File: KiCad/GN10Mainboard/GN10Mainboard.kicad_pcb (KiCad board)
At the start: 4 copper layers, 70 x 50 mm, 106 parts, among them J1 XT30PW-M, J10 Conn_01x05_Socket, J2 Conn_01x02_Pin, J3 USB_C_Receptacle_USB2.0_16P, J4 Conn_01x04, J5 Conn_01x04, J6 Conn_01x04, J7 Conn_01x04, J8 Conn_01x04, J9 Conn_01x06, SW1 SW_Push, SW2 SW_DIP_x04, SW3 SW_Push, U1 OKL-T/x-W5N-C, U2 3.3V, U3 STM32G474RCTx, U4 TBD62083AFNG, U5 7segmentLED, U6 RNBD451, U7 FT231XS, U8 MCP2562-E-SN, U9 MCP2562-E-SN, Y1 24MHz, Y2 32.768kHz

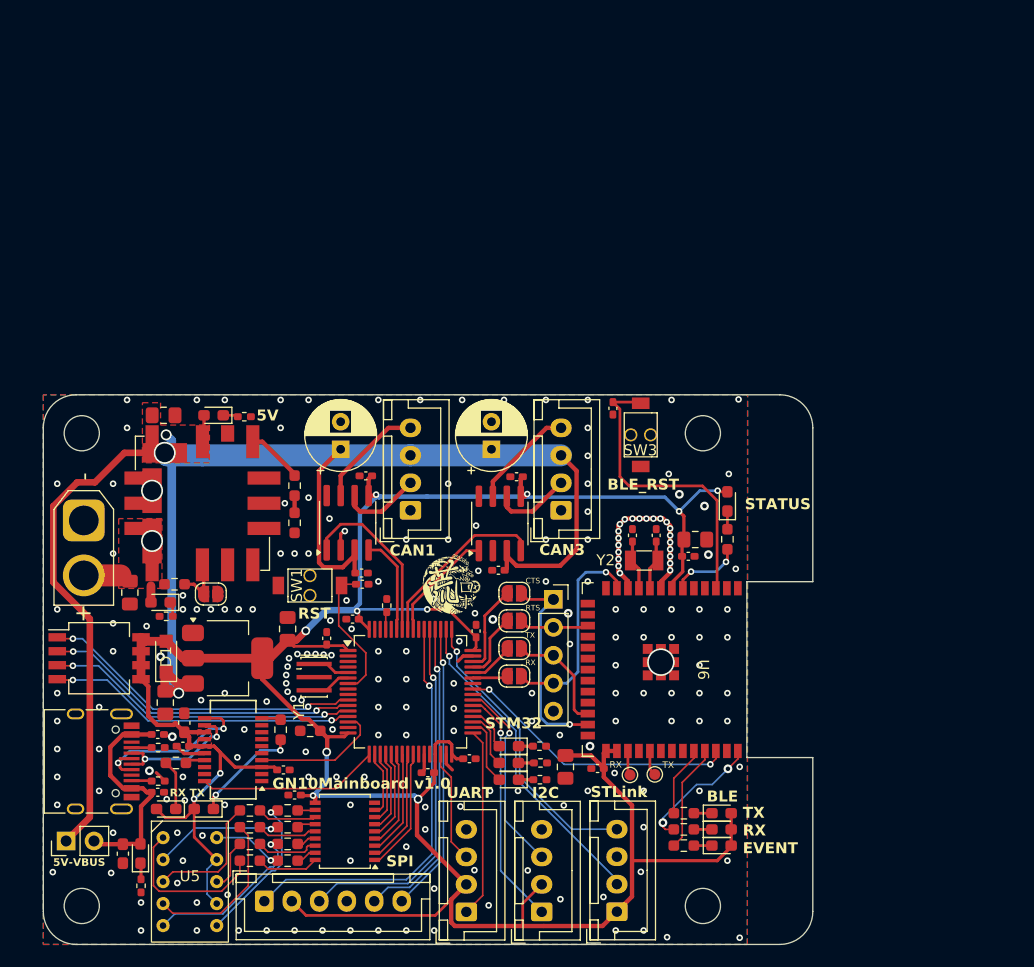
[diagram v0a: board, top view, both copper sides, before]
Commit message: Optimized PCB layout for better noise suppression
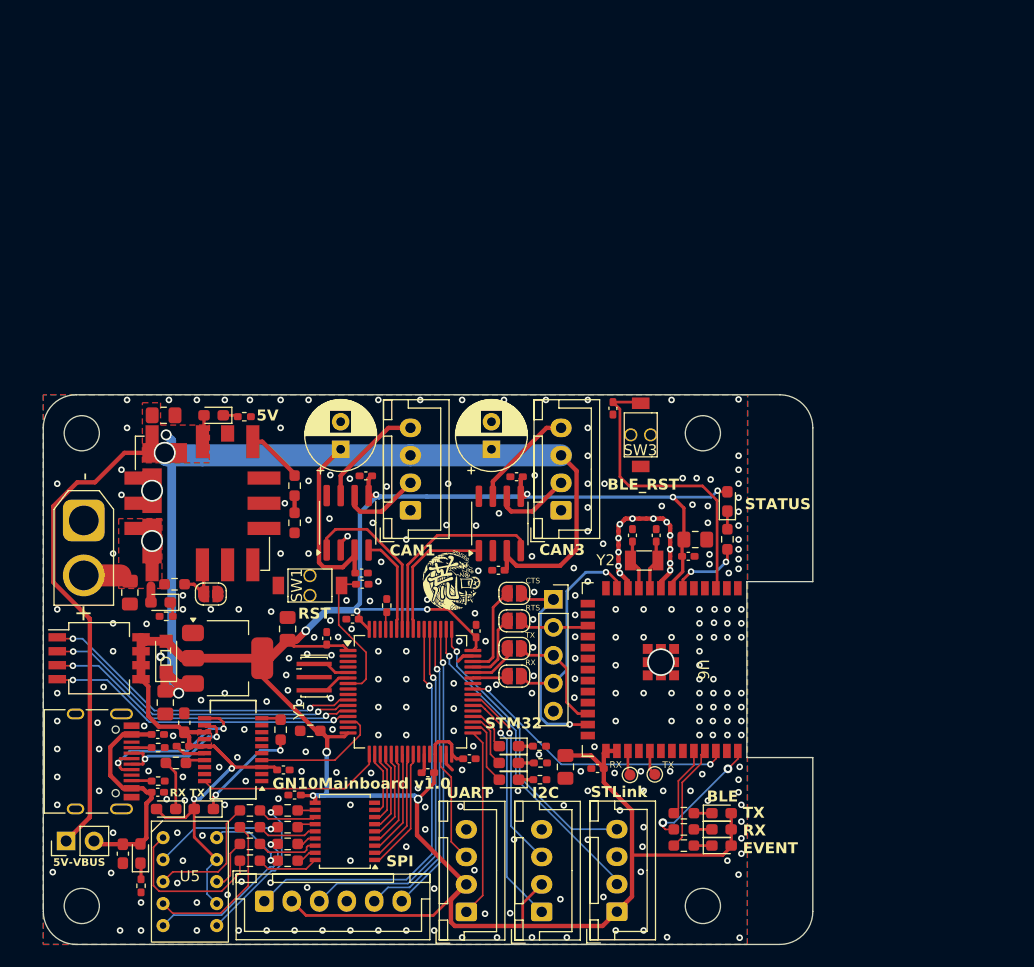
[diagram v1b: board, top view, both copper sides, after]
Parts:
- moved G*** 0.36 mm to (167.0, 117.1)
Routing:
- net +3.3V: track 284.1 -> 286.5 mm
- net CAN3_RX: track 10.3 -> 12.3 mm
- net CAN3_TX: track 16.4 -> 18.4 mm
- net GND: track 28.5 -> 26.8 mm, vias 211 -> 287
- net LED_B_DRV: track 6.41 -> 7.20 mm
- net BLE_UART_RX: track 19.0 -> 18.3 mm

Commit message: 2layer PCB version
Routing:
- removed copper zone on In1.Cu, net GND
- removed copper zone on In2.Cu, net GND
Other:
- copper layers 4 -> 2
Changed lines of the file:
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@@
 	(layers
 		(0 "F.Cu" signal)
-		(1 "In1.Cu" signal)
-		(2 "In2.Cu" signal)
 		(31 "B.Cu" signal)
 		(32 "B.Adhes" user "B.Adhesive")
@@
 			)
 			(layer "dielectric 1"
-				(type "prepreg")
-				(thickness 0.1)
-				(material "FR4")
-				(epsilon_r 4.5)
-				(loss_tangent 0.02)
-			)
-			(layer "In1.Cu"
-				(type "copper")
-				(thickness 0.035)
-			)
-			(layer "dielectric 2"
 				(type "core")
-				(thickness 1.24)
-				(material "FR4")
-				(epsilon_r 4.5)
-				(loss_tangent 0.02)
-			)
-			(layer "In2.Cu"
-				(type "copper")
-				(thickness 0.035)
-			)
-			(layer "dielectric 3"
-				(type "prepreg")
-				(thickness 0.1)
+				(thickness 1.51)
 				(material "FR4")
 				(epsilon_r 4.5)
@@
 			(drillshape 0)
 			(scaleselection 1)
-			(outputdirectory "GN10Mainboard_4layer_v1.0")
+			(outputdirectory "GN10Mainboard_2layer_v1.0")
 		)
 	)
@@
 		(net 1)
 		(net_name "GND")
-		(layers "F.Cu" "In1.Cu" "In2.Cu" "B.Cu")
+		(layers "F&B.Cu")
 		(hatch edge 0.5)
 		(connect_pads thru_hole_only
@@
 		(net 0)
 		(net_name "")
-		(layers "F.Cu" "In1.Cu" "In2.Cu" "B.Cu" "Cmts.User")
+		(layers "F&B.Cu" "Cmts.User")
 		(hatch edge 0.5)
 		(connect_pads

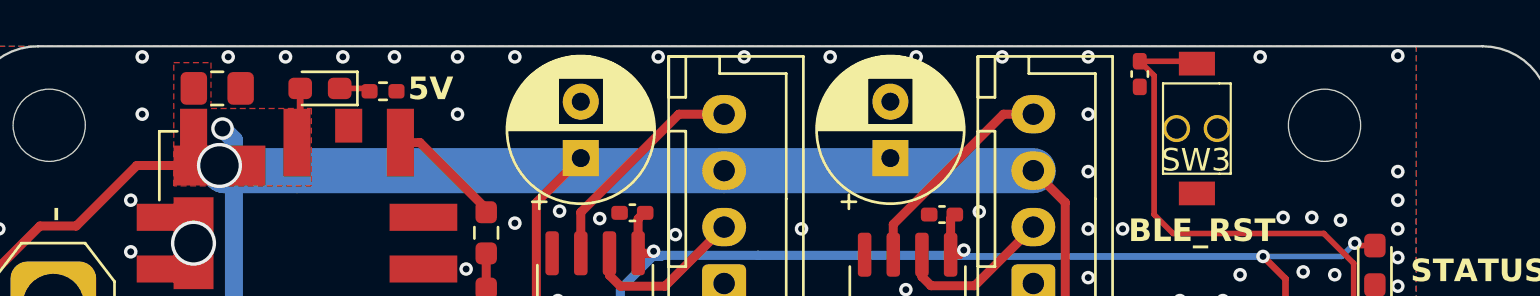
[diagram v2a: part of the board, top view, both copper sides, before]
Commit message: fix: PCB design rules.
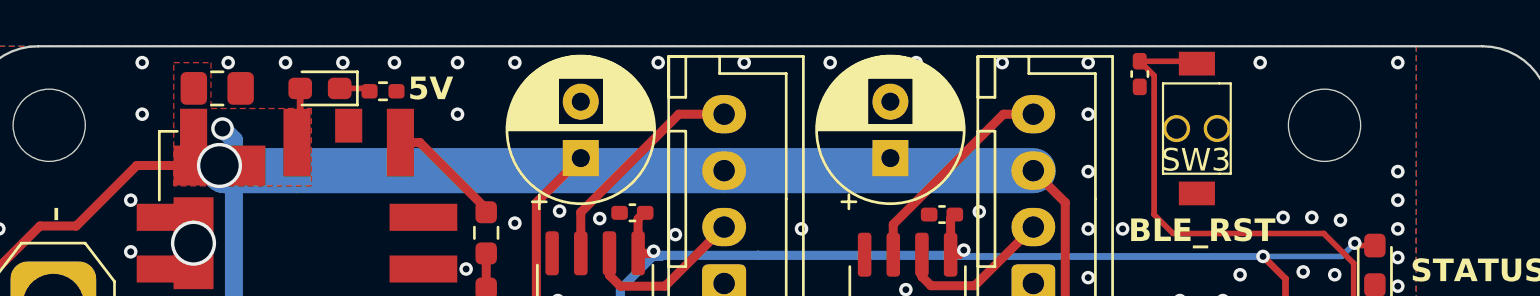
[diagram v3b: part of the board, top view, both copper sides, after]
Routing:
- added copper zone on In1.Cu, net GND
- added copper zone on In2.Cu, net GND
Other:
- copper layers 2 -> 4
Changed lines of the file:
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@@
 	(layers
 		(0 "F.Cu" signal)
+		(1 "In1.Cu" signal)
+		(2 "In2.Cu" signal)
 		(31 "B.Cu" signal)
 		(32 "B.Adhes" user "B.Adhesive")
@@
 			)
 			(layer "dielectric 1"
+				(type "prepreg")
+				(thickness 0.1)
+				(material "FR4")
+				(epsilon_r 4.5)
+				(loss_tangent 0.02)
+			)
+			(layer "In1.Cu"
+				(type "copper")
+				(thickness 0.035)
+			)
+			(layer "dielectric 2"
 				(type "core")
-				(thickness 1.51)
+				(thickness 1.24)
+				(material "FR4")
+				(epsilon_r 4.5)
+				(loss_tangent 0.02)
+			)
+			(layer "In2.Cu"
+				(type "copper")
+				(thickness 0.035)
+			)
+			(layer "dielectric 3"
+				(type "prepreg")
+				(thickness 0.1)
 				(material "FR4")
 				(epsilon_r 4.5)
@@
 			(drillshape 0)
 			(scaleselection 1)
-			(outputdirectory "GN10Mainboard_2layer_v1.0")
+			(outputdirectory "GN10Mainboard_4layer_v1.0")
 		)
 	)
@@
 	)
 	(via
-		(at 137.62 100.47)
+		(at 137.62 100.724)
 		(size 0.6)
 		(drill 0.3)
@@
 	)
 	(via
-		(at 171.91 100.47)
+		(at 171.91 100.724)
 		(size 0.6)
 		(drill 0.3)
@@
 	)
 	(via
-		(at 193.246 100.4192)
+		(at 193.246 100.724)
 		(size 0.6)
 		(drill 0.3)
@@
 	)
 	(via
-		(at 148.796 100.47)
+		(at 148.796 100.724)
 		(size 0.6)
 		(drill 0.3)
@@
 	)
 	(via
-		(at 168.1 100.47)
+		(at 168.1 100.724)
 		(size 0.6)
 		(drill 0.3)
@@
 	)
 	(via
-		(at 179.53 100.47)
+		(at 179.53 100.724)
 		(size 0.6)
 		(drill 0.3)
@@
 	)
 	(via
-		(at 141.43 100.47)
+		(at 141.43 100.724)
 		(size 0.6)
 		(drill 0.3)
@@
 	)
 	(via
-		(at 164.29 100.47)
+		(at 164.29 100.724)
 		(size 0.6)
 		(drill 0.3)
@@
 	)
 	(via
-		(at 160.48 100.47)
+		(at 160.48 100.724)
 		(size 0.6)
 		(drill 0.3)
@@
 	)
 	(via
-		(at 143.97 100.47)
+		(at 143.97 100.724)
 		(size 0.6)
 		(drill 0.3)
@@
 	)
 	(via
-		(at 187.15 100.47)
+		(at 187.15 100.724)
 		(size 0.6)
 		(drill 0.3)
@@
 	)
 	(via
-		(at 154.13 100.47)
+		(at 154.13 100.724)
 		(size 0.6)
 		(drill 0.3)
@@
 	)
 	(via
-		(at 146.51 100.47)
+		(at 146.51 100.724)
 		(size 0.6)
 		(drill 0.3)
@@
 	)
 	(via
-		(at 175.72 100.47)
+		(at 175.72 100.724)
 		(size 0.6)
 		(drill 0.3)
@@
 	)
 	(via
-		(at 151.59 100.47)
+		(at 151.59 100.724)
 		(size 0.6)
 		(drill 0.3)
@@
 		(net 1)
 		(net_name "GND")
-		(layers "F&B.Cu")
+		(layers "F.Cu" "In1.Cu" "In2.Cu" "B.Cu")
 		(hatch edge 0.5)
 		(connect_pads thru_hole_only

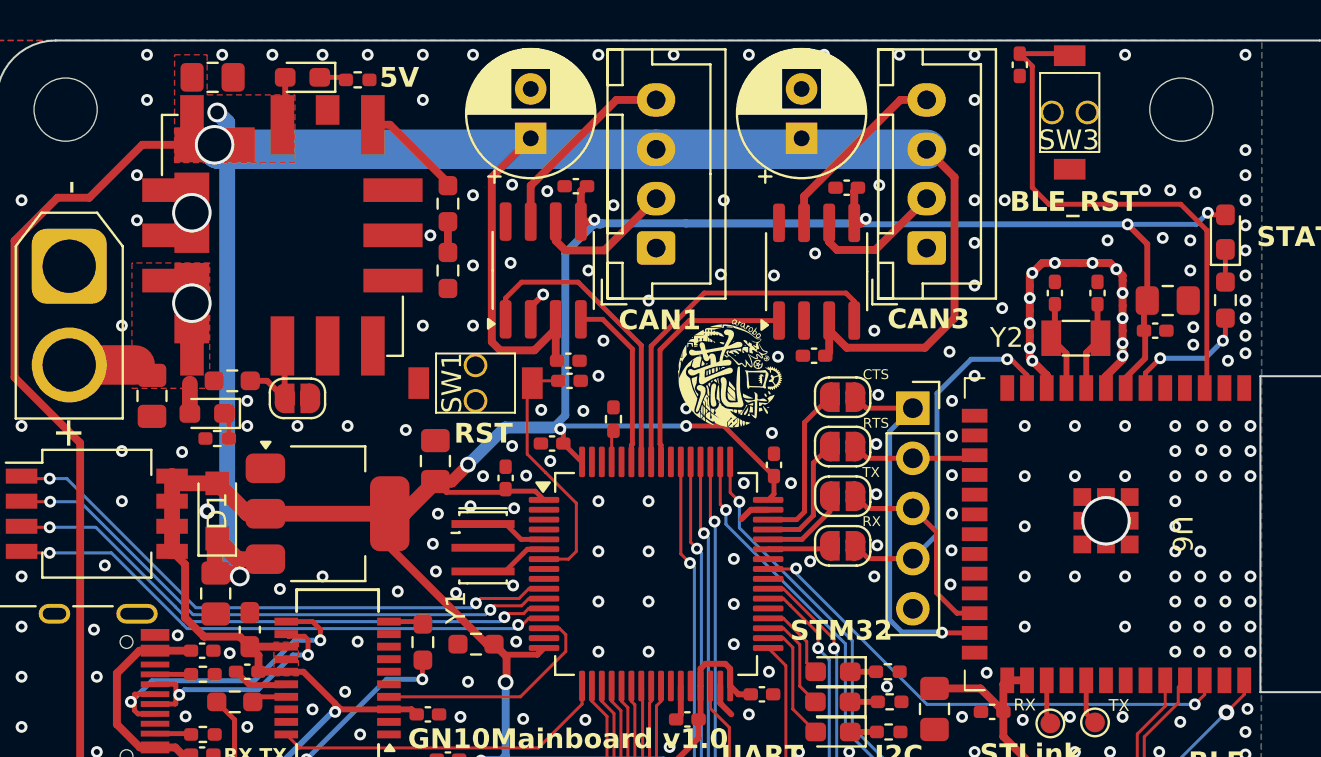
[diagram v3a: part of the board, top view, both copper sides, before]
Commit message: fix:CAN tx/rx pin & silkscreen
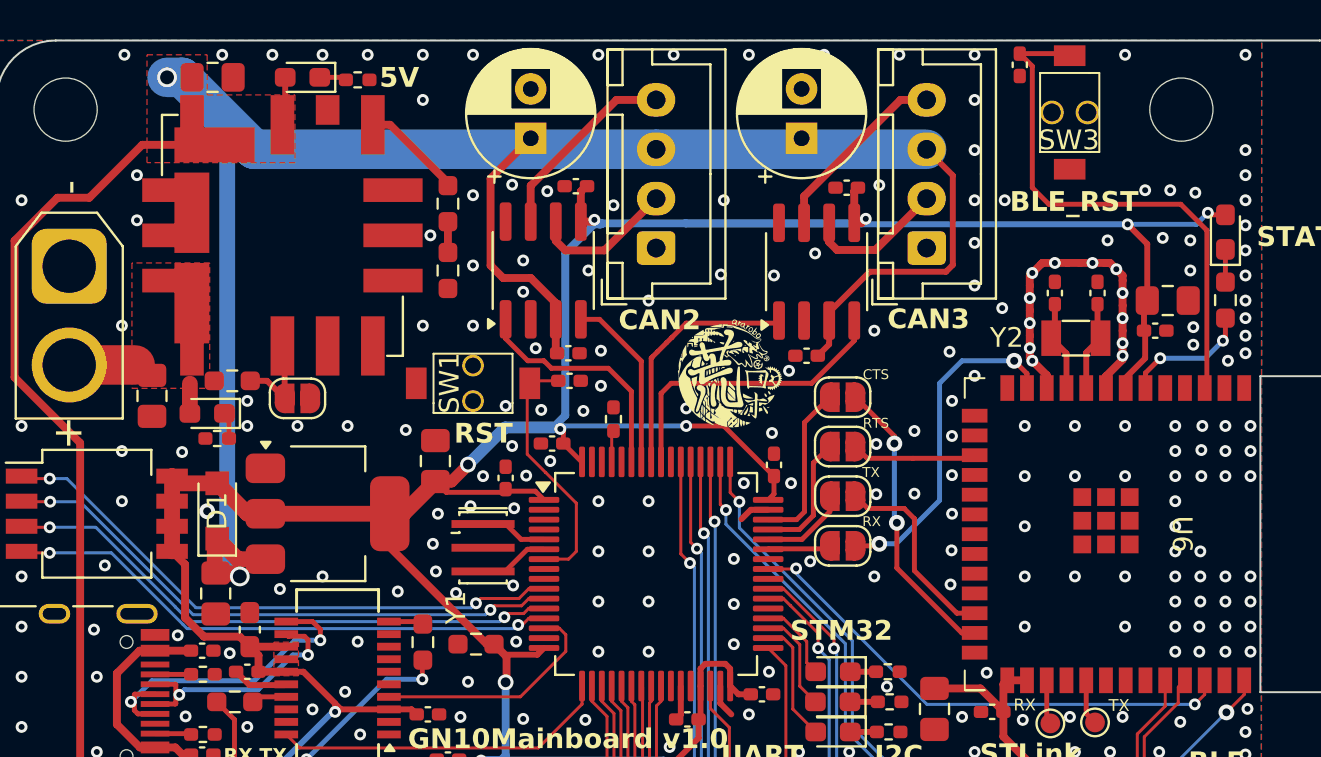
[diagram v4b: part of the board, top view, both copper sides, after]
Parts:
- removed J10: Conn_01x05_Socket, Connector_PinSocket_2.54mm:PinSocket_1x05_P2.54mm_Vertical
- moved C28 0.38 mm to (159.0, 115.8)
- moved C31 0.38 mm to (171.0, 116.0)
- moved SW1 0.13 mm to (154.1, 117.4)
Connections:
- U8 pad 1: CAN2_RX -> CAN2_TX
- U8 pad 4: CAN2_TX -> CAN2_RX
- U9 pad 1: CAN3_RX -> CAN3_TX
- U9 pad 4: CAN3_TX -> CAN3_RX
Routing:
- net CAN2_RX: track 15.5 -> 9.04 mm
- net CAN3_TX: track 18.4 -> 12.5 mm
- net BLE_UART_CTS: track 18.9 -> 14.8 mm, vias 1 -> 2
- net +5V: track 149.9 -> 146.6 mm, vias 3 -> 2
- net CAN2_TX: track 8.97 -> 12.0 mm
- net CAN3_RX: track 12.3 -> 15.4 mm
- net GND: track 26.8 -> 25.3 mm, vias 287 -> 286
- net BLE_UART_RX: track 18.3 -> 17.0 mm, vias 1 -> 2
- net +BATT: vias 1 -> 0
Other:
- board text added: "CAN2"
- board text removed: "CAN1"

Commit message: garber
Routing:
- net GND: vias 286 -> 287
- removed copper zone on In1.Cu, net GND
- removed copper zone on In2.Cu, net GND
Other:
- copper layers 4 -> 2
- board text added: "GN10Mainboard v1.1"
- board text removed: "GN10Mainboard v1.0"
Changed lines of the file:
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@@
 	(layers
 		(0 "F.Cu" signal)
-		(4 "In1.Cu" signal)
-		(6 "In2.Cu" signal)
 		(2 "B.Cu" signal)
 		(9 "F.Adhes" user "F.Adhesive")
@@
 			)
 			(layer "dielectric 1"
-				(type "prepreg")
-				(thickness 0.1)
-				(material "FR4")
-				(epsilon_r 4.5)
-				(loss_tangent 0.02)
-			)
-			(layer "In1.Cu"
-				(type "copper")
-				(thickness 0.035)
-			)
-			(layer "dielectric 2"
 				(type "core")
-				(thickness 1.24)
-				(material "FR4")
-				(epsilon_r 4.5)
-				(loss_tangent 0.02)
-			)
-			(layer "In2.Cu"
-				(type "copper")
-				(thickness 0.035)
-			)
-			(layer "dielectric 3"
-				(type "prepreg")
-				(thickness 0.1)
+				(thickness 1.51)
 				(material "FR4")
 				(epsilon_r 4.5)
@@
 			(drillshape 0)
 			(scaleselection 1)
-			(outputdirectory "GN10Mainboard_4layer_v1.0")
+			(outputdirectory "GN10Mainboard_2layer_v1.0")
 		)
 	)
@@
 			(net 0)
 			(net_name "")
-			(layers "F.Cu" "B.Cu" "In1.Cu" "In2.Cu")
+			(layers "F.Cu" "B.Cu")
 			(hatch full 0.5)
 			(connect_pads
@@
 			(net 0)
 			(net_name "")
-			(layers "F.Cu" "B.Cu" "In1.Cu" "In2.Cu")
+			(layers "F.Cu" "B.Cu")
 			(hatch edge 0.5)
 			(connect_pads
@@
 			(net 0)
 			(net_name "")
-			(layers "F.Cu" "B.Cu" "In1.Cu" "In2.Cu")
+			(layers "F.Cu" "B.Cu")
 			(hatch edge 0.5)
 			(connect_pads
@@
 			(net 0)
 			(net_name "")
-			(layers "F.Cu" "B.Cu" "In1.Cu" "In2.Cu")
+			(layers "F.Cu" "B.Cu")
 			(hatch edge 0.5)
 			(connect_pads
@@
 		)
 	)
-	(gr_text "GN10Mainboard v1.0"
+	(gr_text "GN10Mainboard v1.1"
 		(at 150.828 135.9538 0)
 		(layer "F.SilkS")
@@
 	)
 	(via
+		(at 163.782 116.853)
+		(size 0.6)
+		(drill 0.3)
+		(layers "F.Cu" "B.Cu")
+		(free yes)
+		(net 1)
+	)
+	(via
 		(at 180.9524 145.682)
 		(size 0.6)
@@
 	)
 	(via
+		(at 162.893 115.329)
+		(size 0.6)
+		(drill 0.3)
+		(layers "F.Cu" "B.Cu")
+		(free yes)
+		(net 1)
+	)
+	(via
 		(at 160.48 100.724)
 		(size 0.6)
@@
 	)
 	(via
-		(at 174.5516 120.4344)
-		(size 0.6)
-		(drill 0.3)
-		(layers "F.Cu" "B.Cu")
-		(free yes)
-		(net 1)
-	)
-	(via
 		(at 189.69 124.6)
 		(size 0.6)
@@
 	(via
 		(at 138.636 101.867)
-		(size 1)
-		(drill 0.7)
+		(size 1.2)
+		(drill 0.9)
 		(layers "F.Cu" "B.Cu")
 		(net 3)
@@
 	)
 	(segment
-		(start 177.1 105.51)
+		(start 143.041 105.51)
 		(end 163.401 105.51)
 		(width 2)
@@
 	)
 	(segment
-		(start 139.398 101.867)
-		(end 143.041 105.51)
+		(start 177.1 105.51)
+		(end 163.401 105.51)
 		(width 2)
 		(layer "B.Cu")
@@
 	)
 	(segment
-		(start 138.636 101.867)
-		(end 139.398 101.867)
+		(start 139.398 101.867)
+		(end 143.041 105.51)
 		(width 2)
 		(layer "B.Cu")
@@
 	)
 	(segment
-		(start 143.041 105.51)
-		(end 163.401 105.51)
+		(start 138.636 101.867)
+		(end 139.398 101.867)
 		(width 2)
 		(layer "B.Cu")
@@
 		(net 1)
 		(net_name "GND")
-		(layers "F.Cu" "B.Cu" "In1.Cu" "In2.Cu")
+		(layers "F.Cu" "B.Cu")
 		(hatch edge 0.5)
 		(connect_pads thru_hole_only
